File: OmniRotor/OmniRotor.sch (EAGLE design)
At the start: 118 parts, among them CON1 SPI, CON2 Telem, CON3 I2C, CON4 ADC, CON5 RC_IN, CON6 GPS, Q1 12MHz, U1 MAG3110, U2 LPS331AP, U3 HMC5883L, U4 BMP180, U6 XOR, U7 STM32F405RG, U8 LP2985-3.3, U9 LP2985-3.3

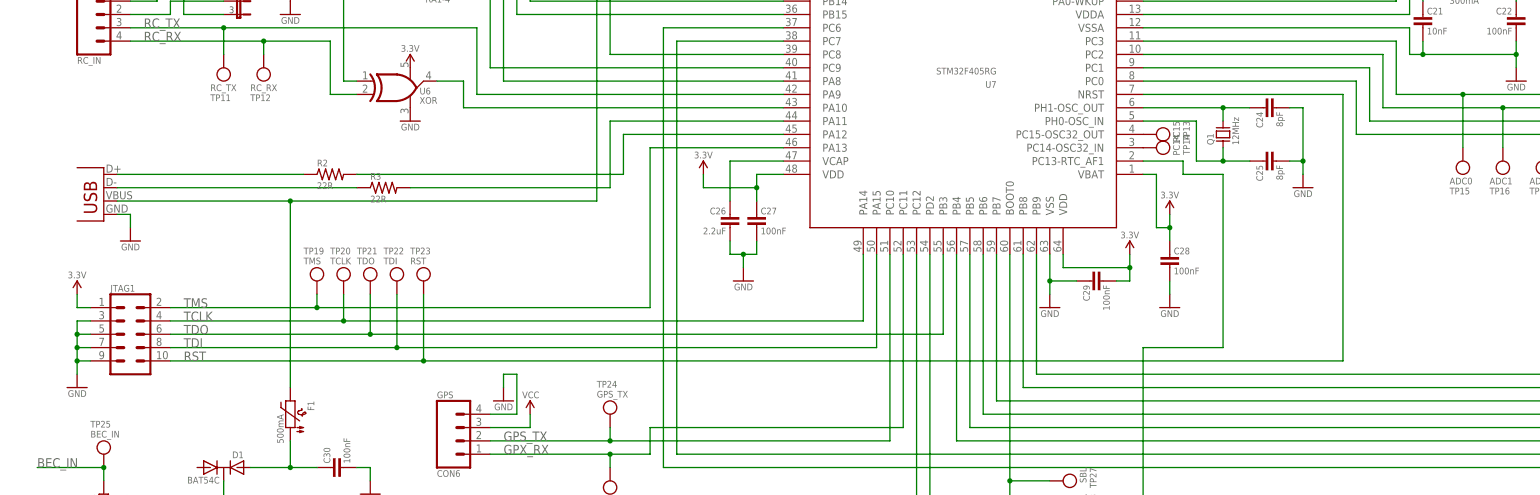
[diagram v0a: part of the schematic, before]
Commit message: Changed debug interface from JTAG to SWD.
Frees up 2 GPIO. Also added pull-up and decoupling cap to reset line.
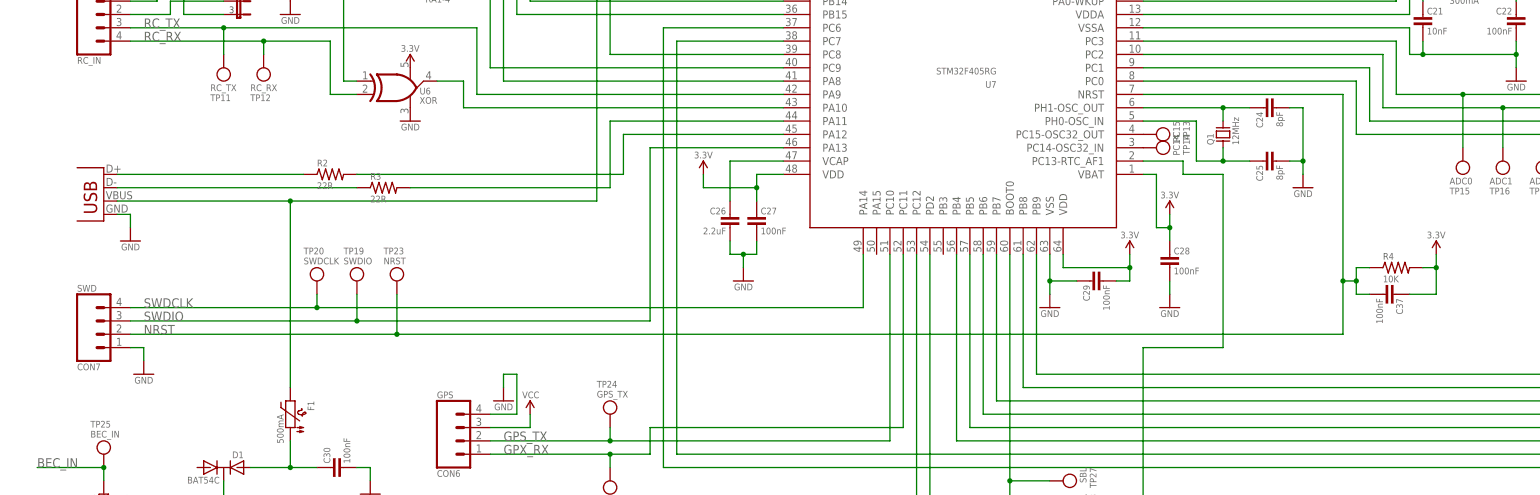
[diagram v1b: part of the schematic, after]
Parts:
- removed JTAG1: JTAGSWD, OmniLoco:JTAGSWD
- removed TP21: TDO, OmniLoco:TESTPOINTROUND0.7MM
- removed TP22: TDI, OmniLoco:TESTPOINTROUND0.7MM
- added C37: 100nF, OmniLoco:CAPACITOR0402
- added CON7: SWD, OmniLoco:M04JST-SH-TOP
- added R4: 10K, OmniLoco:RESISTOR0402
- TP19: value TMS -> SWDIO
- TP20: value TCLK -> SWDCLK
- TP23: value RST -> NRST
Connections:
- removed net RST: JTAG1.10, TP23.1, U7.NRST
- removed net TCLK: JTAG1.4, TP20.1, U7.PA14
- removed net TDI: JTAG1.8, TP22.1, U7.PA15
- removed net TDO: JTAG1.6, TP21.1, U7.PB3
- removed net TMS: JTAG1.2, TP19.1, U7.PA13
- new net NRST: C37.2, CON7.2, R4.1, TP23.1, U7.NRST
- new net SWDCLK: CON7.4, TP20.1, U7.PA14
- new net SWDIO: CON7.3, TP19.1, U7.PA13
- net 3.3V: now also C37.1, R4.2; no longer JTAG1.1
- net GND: now also CON7.1; no longer JTAG1.3, JTAG1.5, JTAG1.7, JTAG1.9
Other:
- moved on the sheet: TP19, TP20, TP23

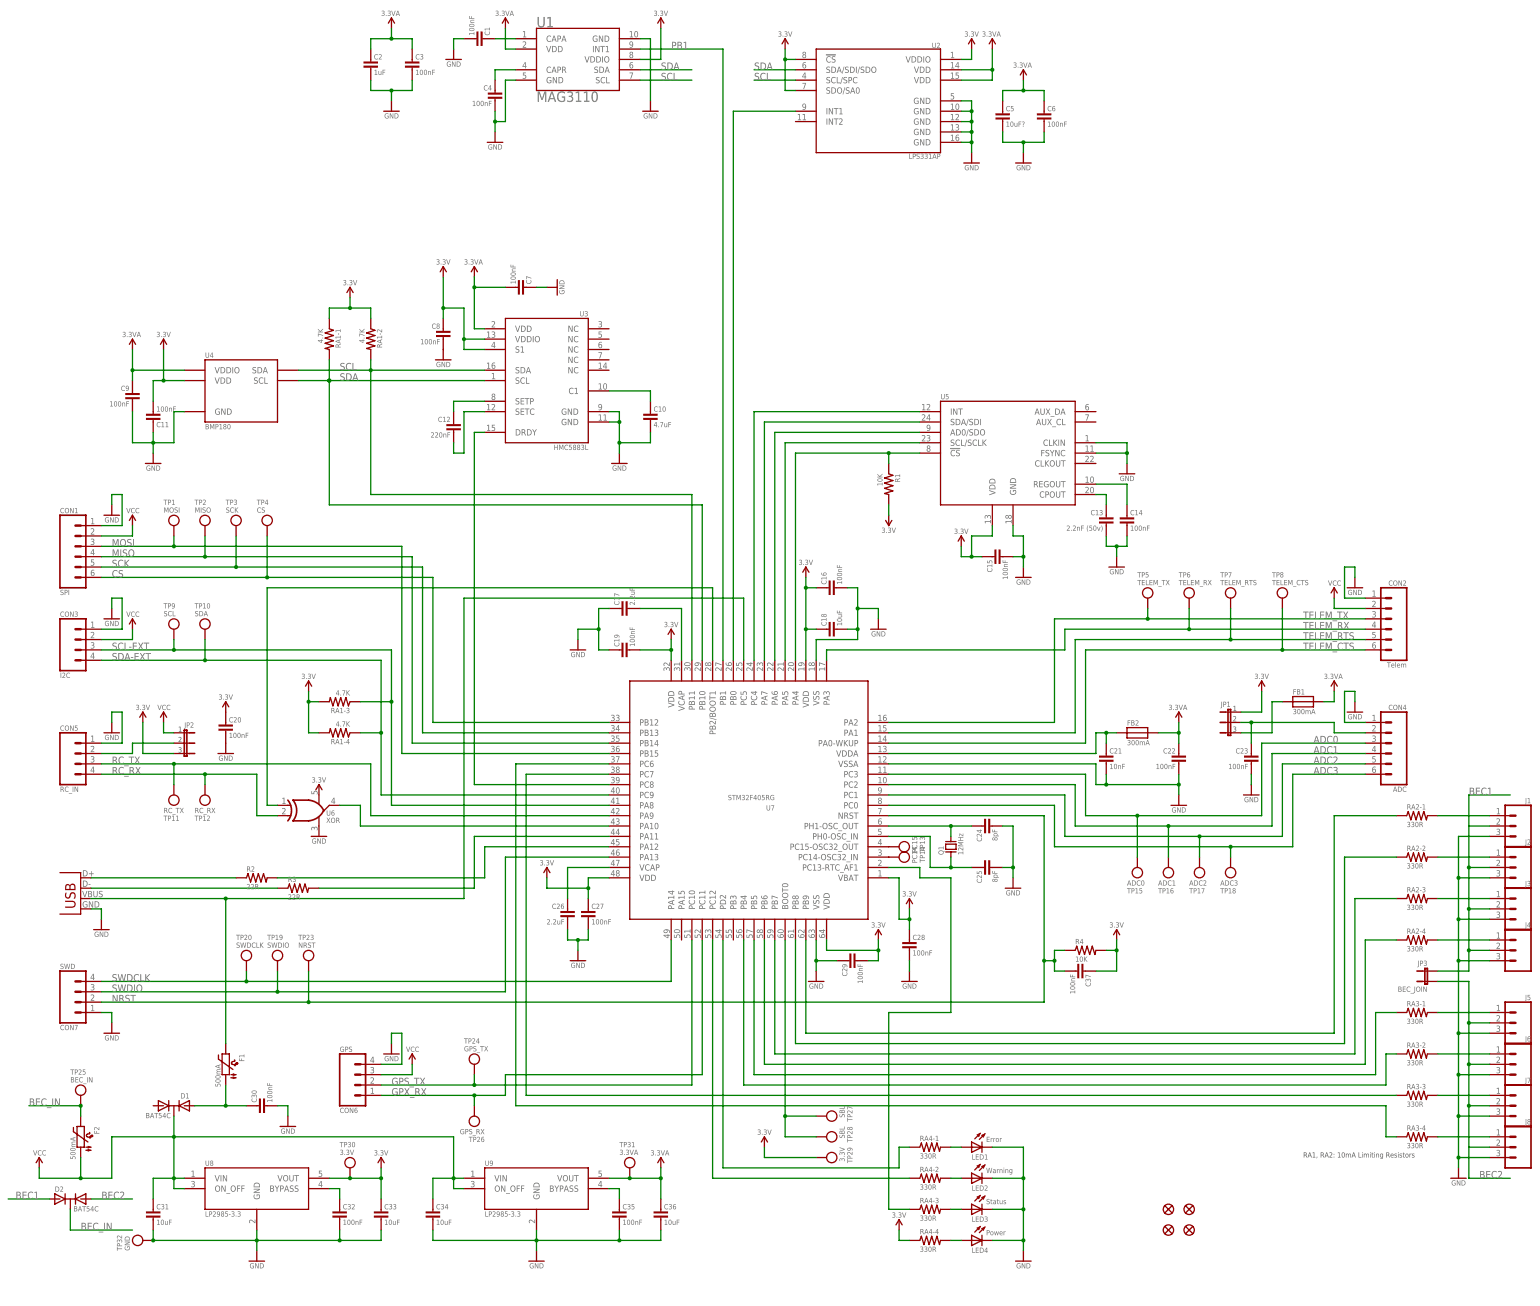
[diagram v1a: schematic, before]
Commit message: More updates for Q4 2012 production.
- Added MS5611 pressure sensor
- Removed MAG3110
- Remapped some I/O pins
- Added additional UART connector
- Added Utility connector (PWM+ADC+SPI)
- Cleaned up all routing
- Moved magnetometer, fixed ground planes
- Changed PTC to 1210 package
- Re-aligned lightpipes
- Remapped most servo IO for maximum flexibility in other peripherals
- Replaced TX pin on RC Input connector with 3.3V, removed voltage
select jumper
- Changed crystal package and frequency
- Added 2.5x3.2mm crystal footprint
- Added lightpipe only footprint
- Removed lightpipe+LED conbimed footprint
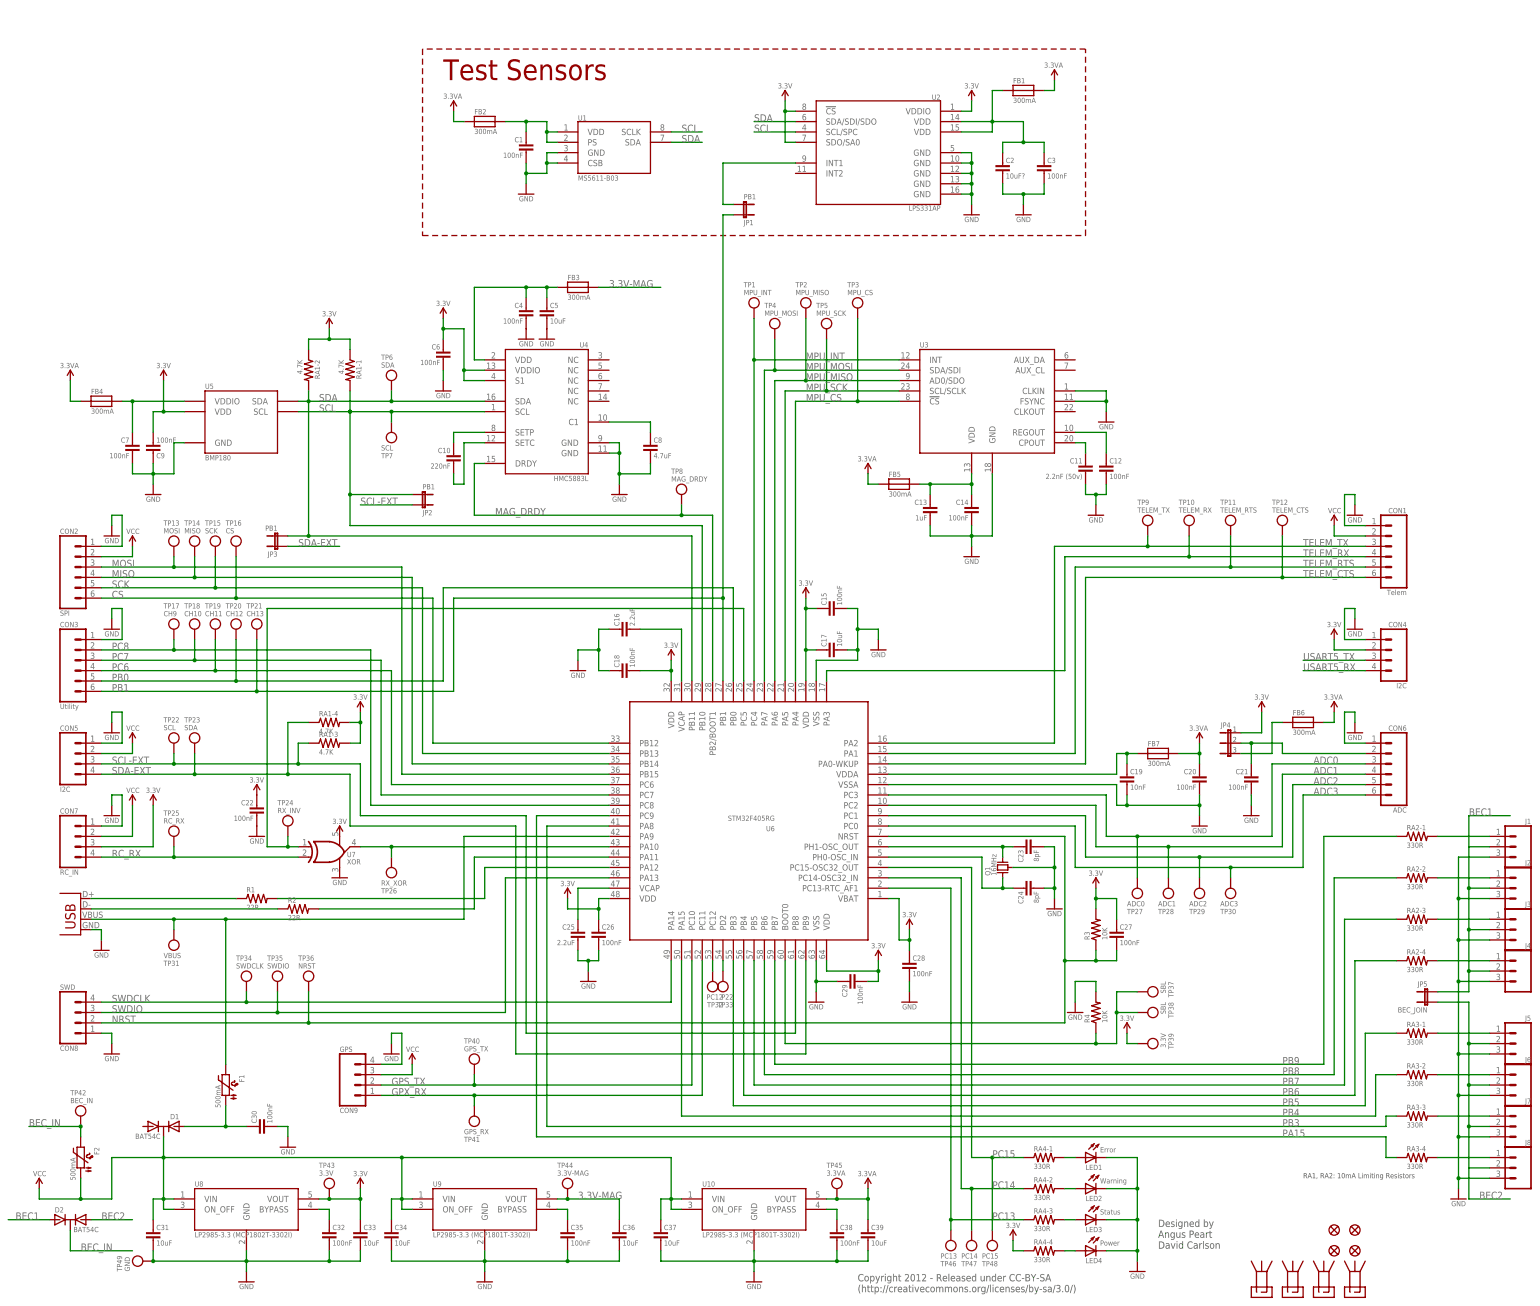
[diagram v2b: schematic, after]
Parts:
- added C38: 100nF, OmniLoco:CAPACITOR0402
- added C39: 10uF, OmniLoco:CAPACITOR-CERAMIC0805
- added CON8: SWD, OmniLoco:M04JST-SH-TOP
- added CON9: GPS, OmniLoco:M04JST-SH-SIDE
- added FB3, FB4, FB5, FB6, FB7: 300mA, OmniLoco:FERRITE0603
- added JP4: (no value), OmniLoco:JUMPER-31-2
- added JP5: BEC_JOIN, OmniLoco:JUMPER-2NO
- added LP1, LP2, LP3, LP4: LIGHTPIPE, OmniLoco:LIGHTPIPE
- added TP21: CH13, OmniLoco:TESTPOINTROUND0.7MM
- added TP22: SCL, OmniLoco:TESTPOINTROUND0.7MM
- added TP33: P22, OmniLoco:TESTPOINTROUND0.7MM
- added TP34: SWDCLK, OmniLoco:TESTPOINTROUND0.7MM
- added TP35: SWDIO, OmniLoco:TESTPOINTROUND0.7MM
- added TP36: NRST, OmniLoco:TESTPOINTROUND0.7MM
- added TP37: SBL, OmniLoco:TESTPOINTROUND1MM
- added TP38: SBL, OmniLoco:TESTPOINTROUND1.5MM
- added TP39: 3.3V, OmniLoco:TESTPOINTROUND1.5MM
- added TP40: GPS_TX, OmniLoco:TESTPOINTROUND0.7MM
- added TP41: GPS_RX, OmniLoco:TESTPOINTROUND0.7MM
- added TP42: BEC_IN, OmniLoco:TESTPOINTROUND0.7MM
- added TP43: 3.3V, OmniLoco:TESTPOINTROUND0.7MM
- added TP44: 3.3V-MAG, OmniLoco:TESTPOINTROUND0.7MM
- added TP45: 3.3VA, OmniLoco:TESTPOINTROUND0.7MM
- added TP46: PC13, OmniLoco:TESTPOINTROUND0.7MM
- added TP47: PC14, OmniLoco:TESTPOINTROUND0.7MM
- added TP48: PC15, OmniLoco:TESTPOINTROUND0.7MM
- added TP49: GND, OmniLoco:TESTPOINTROUND1.5MM
- added U10: LP2985-3.3 (MCP1801T-3302I), OmniLoco:LP2985
- C10: value 4.7uF -> 220nF; device OmniLoco:CAPACITOR0603 -> OmniLoco:CAPACITOR0402
- C11: value 100nF -> 2.2nF (50v)
- C12: value 220nF -> 100nF
- C13: value 2.2nF (50v) -> 1uF; device OmniLoco:CAPACITOR0402 -> OmniLoco:CAPACITOR0603
- C16: value 100nF -> 2.2uF; device OmniLoco:CAPACITOR0402 -> OmniLoco:CAPACITOR0603
- C17: value 2.2uF -> 10uF; device OmniLoco:CAPACITOR0603 -> OmniLoco:CAPACITOR-CERAMIC0805
- C18: value 10uF -> 100nF; device OmniLoco:CAPACITOR-CERAMIC0805 -> OmniLoco:CAPACITOR0402
- C19: value 100nF -> 10nF
- C2: value 1uF -> 10uF?
- C21: value 10nF -> 100nF
- C23: value 100nF -> 8pF
- C25: value 8pF -> 2.2uF; device OmniLoco:CAPACITOR0402 -> OmniLoco:CAPACITOR0603
- C26: value 2.2uF -> 100nF; device OmniLoco:CAPACITOR0603 -> OmniLoco:CAPACITOR0402
- C37: value 100nF -> 10uF; device OmniLoco:CAPACITOR0402 -> OmniLoco:CAPACITOR-CERAMIC0805
- C5: value 10uF? -> 10uF; device OmniLoco:CAPACITOR0603 -> OmniLoco:CAPACITOR0805
- C8: value 100nF -> 4.7uF; device OmniLoco:CAPACITOR0402 -> OmniLoco:CAPACITOR0603
- CON1: value SPI -> Telem
- CON2: value Telem -> SPI
- CON3: value I2C -> Utility; device OmniLoco:M04JST-SH-SIDE -> OmniLoco:M06JST-SH-SIDE
- CON4: value ADC -> I2C; device OmniLoco:M06JST-SH-SIDE -> OmniLoco:M04JST-SH-SIDE
- CON5: value RC_IN -> I2C
- CON6: value GPS -> ADC; device OmniLoco:M04JST-SH-SIDE -> OmniLoco:M06JST-SH-SIDE
- CON7: value SWD -> RC_IN; device OmniLoco:M04JST-SH-TOP -> OmniLoco:M04JST-SH-SIDE
- F1, F2: device OmniLoco:PTC1812 -> OmniLoco:PTC1210
- JP1: value (none) -> PB1; device OmniLoco:JUMPER-31-2 -> OmniLoco:JUMPER-2NO
- JP2: value (none) -> PB1; device OmniLoco:JUMPER-32-3 -> OmniLoco:JUMPER-2NO
- JP3: value BEC_JOIN -> PB1
- LED1, LED2, LED3, LED4: device OmniLoco:LED0603-LP -> OmniLoco:LED0603
- Q1: value 12MHz -> 16MHz; device OmniLoco:CRYSTAL5X3-2 -> OmniLoco:CRYSTAL-GND
- R1: value 10K -> 22R
- R3: value 22R -> 10K
- TP1: value MOSI -> MPU_INT
- TP10: value SDA -> TELEM_RX
- TP11: value RC_TX -> TELEM_RTS
- TP12: value RC_RX -> TELEM_CTS
- TP13: value PC15 -> MOSI
- TP14: value PC14 -> MISO
- TP15: value ADC0 -> SCK
- TP16: value ADC1 -> CS
- TP17: value ADC2 -> CH9
- TP18: value ADC3 -> CH10
- TP19: value SWDIO -> CH11
- TP2: value MISO -> MPU_MISO
- TP20: value SWDCLK -> CH12
- TP23: value NRST -> SDA
- TP24: value GPS_TX -> RX_INV
- TP25: value BEC_IN -> RC_RX; device OmniLoco:TESTPOINTROUND1.5MM -> OmniLoco:TESTPOINTROUND0.7MM
- TP26: value GPS_RX -> RX_XOR
- TP27: value SBL -> ADC0; device OmniLoco:TESTPOINTROUND1MM -> OmniLoco:TESTPOINTROUND0.7MM
- TP28: value SBL -> ADC1; device OmniLoco:TESTPOINTROUND1.5MM -> OmniLoco:TESTPOINTROUND0.7MM
- TP29: value 3.3V -> ADC2; device OmniLoco:TESTPOINTROUND1.5MM -> OmniLoco:TESTPOINTROUND0.7MM
- TP3: value SCK -> MPU_CS
- TP30: value 3.3V -> ADC3
- TP31: value 3.3VA -> VBUS
- TP32: value GND -> PC12; device OmniLoco:TESTPOINTROUND1.5MM -> OmniLoco:TESTPOINTROUND0.7MM
- TP4: value CS -> MPU_MOSI
- TP5: value TELEM_TX -> MPU_SCK
- TP6: value TELEM_RX -> SDA
- TP7: value TELEM_RTS -> SCL
- TP8: value TELEM_CTS -> MAG_DRDY
- TP9: value SCL -> TELEM_TX
- U1: value MAG3110 -> MS5611-B03; device OmniLoco:MAG3110 -> OmniLoco:MS5611
- U3: value HMC5883L -> (none); device OmniLoco:HMC5883L -> OmniLoco:MPU6000
- U4: value BMP180 -> HMC5883L; device OmniLoco:BMP180 -> OmniLoco:HMC5883L
- U5: value (none) -> BMP180; device OmniLoco:MPU6000 -> OmniLoco:BMP180
- U6: value XOR -> STM32F405RG; device OmniLoco:74LVC1G86SC70 -> OmniLoco:STM32FX05R
- U7: value STM32F405RG -> XOR; device OmniLoco:STM32FX05R -> OmniLoco:74LVC1G86SC70
- U8: value LP2985-3.3 -> LP2985-3.3 (MCP1802T-3302I)
- U9: value LP2985-3.3 -> LP2985-3.3 (MCP1801T-3302I)
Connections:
- removed net N$12: C1.1, U1.CAPA
- removed net N$14: U6.I0, U7.PB2/BOOT1
- removed net N$17: R1.1, U5.!CS!, U7.PA4
- removed net N$19: TP13.1, U7.PC15-OSC32_OUT
- removed net N$22: U5.SDA/SDI, U7.PA7
- removed net N$25: U5.AD0/SDO, U7.PA6
- removed net N$27: U5.SCL/SCLK, U7.PA5
- removed net N$28: U5.INT, U7.PC4
- removed net N$42: RA2-4.1, U7.PB6
- removed net N$43: RA2-3.1, U7.PB7
- removed net N$45: RA2-1.1, U7.PB9
- removed net N$47: RA3-1.1, U7.PB5
- removed net N$48: RA3-2.1, U7.PB4
- removed net N$49: RA3-4.1, U7.PC6
- removed net N$50: RA3-3.1, U7.PC7
- removed net N$55: RA4-2.1, U7.PC12
- removed net N$56: RA4-1.1, U7.PD2
- removed net N$57: RA4-3.1, U7.PC13-RTC_AF1
- removed net N$59: C4.1, U1.CAPR
- removed net RC_TX: CON5.3, TP11.1, U7.PA9
- new net 3.3V-MAG: C36.1, FB3.2, TP44.1, U9.VOUT
- new net MAG_DRDY: TP8.1, U4.DRDY, U6.PB2/BOOT1
- new net MPU_CS: TP3.1, U3.!CS!, U6.PA4
- new net MPU_INT: TP1.1, U3.INT, U6.PC4
- new net MPU_MISO: TP2.1, U3.AD0/SDO, U6.PA6
- new net MPU_MOSI: TP4.1, U3.SDA/SDI, U6.PA7
- new net MPU_SCK: TP5.1, U3.SCL/SCLK, U6.PA5
- new net N$51: C38.1, U10.BYPASS
- new net N$54: C4.1, C5.1, FB3.1, U4.VDD
- new net N$58: C7.1, FB4.2, U5.VDDIO
- new net N$64: C1.1, FB2.2, U1.PS, U1.VDD
- new net PA15: RA3-4.1, U6.PC9
- new net PB3: RA3-3.1, U6.PA8
- new net PB4: RA3-2.1, U6.PA15
- new net PB5: RA3-1.1, U6.PB3
- new net PB6: RA2-4.1, U6.PB4
- new net PB7: RA2-3.1, U6.PB5
- new net PB8: RA2-2.1, U6.PB6
- new net PB9: RA2-1.1, U6.PB7
- new net PC13: RA4-3.1, TP46.1, U6.PC13-RTC_AF1
- new net PC14: RA4-2.1, TP47.1, U6.PC14-OSC32_IN
- new net PC15: RA4-1.1, TP48.1, U6.PC15-OSC32_OUT
- new net PC6: CON3.4, TP19.1, U6.PC6
- new net PC7: CON3.3, TP18.1, U6.PC7
- new net PC8: CON3.2, TP17.1, U6.PC8
- new net USART5_RX: CON4.4, TP33.1, U6.PD2
- new net USART5_TX: CON4.3, TP32.1, U6.PC12
- net 3.3V: now also C17.1, C18.2, C22.1, C26.1, C6.1, C9.2, CON4.2, CON7.3, JP4.1, R3.2, TP39.1, TP43.1, U4.S1, U4.VDDIO, U6.VBAT, U6.VDD@1, U6.VDD@2, U6.VDD@3, U6.VDD@4, U7.VCC; no longer C11.2, C16.1, C18.1, C19.2, C20.1, C37.1, C8.1, JP1.1, JP2.3, R1.2, R4.2, TP29.1, TP30.1, U1.VDDIO, U3.S1, U3.VDDIO, U6.VCC, U7.VBAT, U7.VDD@1, U7.VDD@2, U7.VDD@3, U7.VDD@4
- net 3.3VA: now also C20.1, C39.1, FB2.1, FB4.1, FB5.1, FB6.2, FB7.2, TP45.1, U10.VOUT; no longer C2.1, C22.1, C3.1, C36.1, C5.1, C6.1, C7.2, C9.1, FB2.2, TP31.1, U1.VDD, U2.VDD@1, U2.VDD@2, U3.VDD, U4.VDDIO, U9.VOUT
- net ADC0: now also CON6.3, TP27.1, U6.PC3; no longer CON4.3, TP15.1, U7.PC3
- net ADC1: now also CON6.4, TP28.1, U6.PC2; no longer CON4.4, TP16.1, U7.PC2
- net ADC2: now also CON6.5, TP29.1, U6.PC1; no longer CON4.5, TP17.1, U7.PC1
- net ADC3: now also CON6.6, TP30.1, U6.PC0; no longer CON4.6, TP18.1, U7.PC0
- net BEC1: now also JP5.1; no longer JP3.1
- net BEC2: now also JP5.2; no longer JP3.2
- net BEC_IN: now also TP42.1; no longer TP25.1
- net CS: now also CON2.6, TP16.1, U6.PB12; no longer CON1.6, TP4.1, U7.PB12
- net GND: now also C11.2, C12.2, C16.1, C17.2, C18.1, C19.2, C37.2, C38.2, C39.2, C7.2, C9.1, CON6.1, CON8.1, CON9.4, Q1.GND, R4.2, TP49.1, U1.CSB, U1.GND, U10.GND, U3.CLKIN, U3.FSYNC, U3.GND, U4.GND@1, U4.GND@2, U6.VSS@3, U6.VSS@4, U6.VSSA, U7.GND; no longer C10.2, C11.1, C16.2, C17.1, C18.2, C19.1, C27.2, C7.1, C9.2, CON6.4, TP32.1, U1.GND@1, U1.GND@2, U3.GND@1, U3.GND@2, U4.GND, U5.CLKIN, U5.FSYNC, U6.GND, U7.VSS@3, U7.VSS@4, U7.VSSA
- net GPS_TX: now also CON9.2, TP40.1, U6.PC10; no longer CON6.2, TP24.1, U7.PC10
- net GPX_RX: now also CON9.1, TP41.1, U6.PC11; no longer CON6.1, TP26.1, U7.PC11
- net MISO: now also CON2.4, TP14.1, U6.PB14; no longer CON1.4, TP2.1, U7.PB14
- net MOSI: now also CON2.3, TP13.1, U6.PB15; no longer CON1.3, TP1.1, U7.PB15
- net N$1: now also C19.1, FB7.1, U6.VDDA; no longer C21.1, FB2.1, U7.VDDA
- net N$10: now also R2.2, U6.PA11; no longer R3.2, U7.PA11
- net N$11: now also R1.2, U6.PA12; no longer R2.2, U7.PA12
- net N$13: now also TP26.1, U6.PA10, U7.O; no longer U6.O, U7.PA10
- net N$15: now also C10.1, U4.SETP; no longer C12.1, U3.SETP
- net N$16: now also C10.2, U4.SETC; no longer C12.2, U3.SETC
- net N$18: now also C13.1, C14.1, FB5.2, U3.VDD; no longer U3.DRDY, U7.PC8
- net N$2: now also C23.1, U6.PH1-OSC_OUT; no longer C24.1, U7.PH1-OSC_OUT
- net N$20: now also C8.1, U4.C1; no longer C10.1, U3.C1
- net N$21: now also C21.1, CON6.2, JP4.2; no longer C23.1, CON4.2, JP1.2
- net N$23: now also C2.1, C3.1, FB1.1, U2.VDD@1, U2.VDD@2; no longer TP14.1, U7.PC14-OSC32_IN
- net N$29: now also FB6.1, JP4.3; no longer FB1.1, JP1.3
- net N$3: now also C24.1, U6.PH0-OSC_IN; no longer C25.1, U7.PH0-OSC_IN
- net N$31: now also C11.1, U3.CPOUT; no longer C13.1, U5.CPOUT
- net N$32: now also C12.1, U3.REGOUT; no longer C14.1, U5.REGOUT
- net N$44: now also JP1.2, U2.INT1; no longer RA2-2.1, U7.PB8
- net N$46: now also R4.1, TP37.1, TP38.1, U6.BOOT0; no longer TP27.1, TP28.1, U7.BOOT0
- net N$6: now also TP24.1, U6.PC5, U7.I0; no longer CON5.2, JP2.2
- net N$8: now also R1.1; no longer R2.1
- net N$9: now also R2.1; no longer R3.1
- net NRST: now also C27.2, CON8.2, R3.1, TP36.1, U6.NRST; no longer C37.2, CON7.2, R4.1, TP23.1, U7.NRST
- net PB0: now also CON3.5, TP20.1, U6.PB0; no longer U2.INT1, U7.PB0
- net PB1: now also CON3.6, JP1.1, TP21.1, U6.PB1; no longer U1.INT1, U7.PB1
- net RC_RX: now also CON7.4, TP25.1, U7.I1; no longer CON5.4, TP12.1, U6.I1
- net SCK: now also CON2.5, TP15.1, U6.PB13; no longer CON1.5, TP3.1, U7.PB13
- net SCL: now also JP2.2, RA1-1.2, TP7.1, U1.SCLK, U4.SCL, U5.SCL, U6.PB10; no longer RA1-2.2, U1.SCL, U3.SDA, U4.SDA, U7.PB11
- net SCL-EXT: now also CON5.3, JP2.1, TP22.1, U6.PB8; no longer CON3.3, TP9.1, U7.PA8
- net SDA: now also JP3.2, RA1-2.2, TP6.1, U4.SDA, U5.SDA, U6.PB11; no longer RA1-1.2, U3.SCL, U4.SCL, U7.PB10
- net SDA-EXT: now also CON5.4, JP3.1, TP23.1, U6.PB9; no longer CON3.4, TP10.1, U7.PC9
- net SWDCLK: now also CON8.4, TP34.1, U6.PA14; no longer CON7.4, TP20.1, U7.PA14
- net SWDIO: now also CON8.3, TP35.1, U6.PA13; no longer CON7.3, TP19.1, U7.PA13
- net TELEM_CTS: now also CON1.6, TP12.1, U6.PA0-WKUP; no longer CON2.6, TP8.1, U7.PA0-WKUP
- net TELEM_RTS: now also CON1.5, TP11.1, U6.PA1; no longer CON2.5, TP7.1, U7.PA1
- net TELEM_RX: now also CON1.4, TP10.1, U6.PA3; no longer CON2.4, TP6.1, U7.PA3
- net TELEM_TX: now also CON1.3, TP9.1, U6.PA2; no longer CON2.3, TP5.1, U7.PA2
- net VCAP@1: now also C16.2, U6.VCAP@1; no longer C17.2, U7.VCAP@1
- net VCAP@2: now also C25.1, U6.VCAP@2; no longer C26.1, U7.VCAP@2
- net VCC: now also C37.1, CON5.2, CON7.2, CON9.3, U10.ON_OFF, U10.VIN; no longer CON3.2, CON6.3, JP2.1
- net VUSB: now also TP31.1, U6.PA9; no longer U7.PC5
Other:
- note added: "Copyright 2012 - Released under CC-BY-SA (http://creativecommons.org/licenses/by-sa/3.0/)"
- note added: "Designed by Angus Peart David Carlson"
- note added: "Test Sensors"
- moved on the sheet: C1, C10, C11, C12, C13, C14, C15, C16, C17, C18, C19, C2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
